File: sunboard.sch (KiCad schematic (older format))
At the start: 24 parts, among them J1 Barrel_Jack_MountingPin, J2 Conn_01x02, Q1 IRLB8721PBF, SW1 SW_Push, U1 STM32F030C8Tx, U4 MIC5209, Y1 Crystal_Small

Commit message: fixed footprints
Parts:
- removed J1: Barrel_Jack_MountingPin, Connector_BarrelJack:BarrelJack_CUI_PJ-063AH_Horizontal, symbol Connector:Barrel_Jack_MountingPin
- removed Q1: IRLB8721PBF, Package_TO_SOT_THT:TO-220-3_Vertical, symbol Transistor_FET:IRLB8721PBF
- added J3: Barrel_Jack, Connector_BarrelJack:BarrelJack_Horizontal, symbol Connector:Barrel_Jack
- 0.1uF1: footprint Capacitor_SMD:C_0603_1608Metric -> Capacitor_SMD:C_0805_2012Metric
- Y1: symbol Device:Crystal_Small -> Device:Crystal_GND24
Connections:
- net +12V: now also J3.1
- net GND: now also Y1.2, Y1.4, J3.2
- net at 1M1.2, 20pF2.1, U1.6 (PF1): now also Y1.3; no longer Y1.2
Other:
- moved on the sheet: FDD8780
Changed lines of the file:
@@
 $EndDescr
-$Comp
-L Transistor_FET:IRLB8721PBF Q1
-U 1 1 5C4B2BC1
-P 3000 1950
-F 0 "Q1" H 3205 1996 50  0000 L CNN
-F 1 "IRLB8721PBF" H 3205 1905 50  0000 L CNN
-F 2 "Package_TO_SOT_THT:TO-220-3_Vertical" H 3250 1875 50  0001 L CIN
-F 3 "http://www.infineon.com/dgdl/irlb8721pbf.pdf?fileId=5546d462533600a40153566056732591" H 3000 1950 50  0001 L CNN
-	1    3000 1950
-	1    0    0    -1
-$EndComp
-$Comp
-L Connector:Barrel_Jack_MountingPin J1
-U 1 1 5C4B7F75
-P 1250 1700
-F 0 "J1" H 1305 2017 50  0000 C CNN
-F 1 "Barrel_Jack_MountingPin" H 1305 1926 50  0000 C CNN
-F 2 "Connector_BarrelJack:BarrelJack_CUI_PJ-063AH_Horizontal" H 1300 1660 50  0001 C CNN
-F 3 "~" H 1300 1660 50  0001 C CNN
-	1    1250 1700
-	1    0    0    -1
-$EndComp
-$Comp
-L power:+12V #PWR0107
-U 1 1 5C4B8002
-P 1550 1600
-F 0 "#PWR0107" H 1550 1450 50  0001 C CNN
-F 1 "+12V" V 1565 1728 50  0000 L CNN
-F 2 "" H 1550 1600 50  0001 C CNN
-F 3 "" H 1550 1600 50  0001 C CNN
-	1    1550 1600
-	0    1    1    0
-$EndComp
-$Comp
-L power:GND #PWR0110
-U 1 1 5C4B822C
-P 1250 2000
-F 0 "#PWR0110" H 1250 1750 50  0001 C CNN
-F 1 "GND" H 1255 1827 50  0000 C CNN
-F 2 "" H 1250 2000 50  0001 C CNN
-F 3 "" H 1250 2000 50  0001 C CNN
-	1    1250 2000
-	1    0    0    -1
-$EndComp
-$Comp
-L power:GND #PWR0111
-U 1 1 5C4B824B
-P 1550 1800
-F 0 "#PWR0111" H 1550 1550 50  0001 C CNN
-F 1 "GND" H 1555 1627 50  0000 C CNN
-F 2 "" H 1550 1800 50  0001 C CNN
-F 3 "" H 1550 1800 50  0001 C CNN
-	1    1550 1800
-	1    0    0    -1
-$EndComp
 $Comp
 L power:GND #PWR0112
@@
 $EndComp
 $Comp
-L power:GND #PWR0113
-U 1 1 5C4B88F2
-P 3100 2150
-F 0 "#PWR0113" H 3100 1900 50  0001 C CNN
-F 1 "GND" H 3105 1977 50  0000 C CNN
-F 2 "" H 3100 2150 50  0001 C CNN
-F 3 "" H 3100 2150 50  0001 C CNN
-	1    3100 2150
-	1    0    0    -1
-$EndComp
-Wire Wire Line
-	3100 1750 3100 1400
-$Comp
 L MCU_ST_STM32F0:STM32F030C8Tx U1
 U 1 1 5C4B8CC2
@@
 	2050 5100 2250 5100
 $Comp
-L Device:Crystal_Small Y1
+L Device:Crystal_GND24 Y1
 U 1 1 5C4BE6CB
 P 1850 4450
@@
 Wire Wire Line
 	1500 4350 1300 4350
-Wire Wire Line
-	1300 4350 1300 4550
 Connection ~ 1300 4550
 Wire Wire Line
@@
 Text Label 4150 6200 0    50   ~ 0
 PWM
-Wire Wire Line
-	2800 1950 2350 1950
-Text Label 2350 1950 0    50   ~ 0
-PWM
-Text Label 3100 1400 0    50   ~ 0
-LED_GND
 $Comp
 L genLib:MIC5209 U4
@@
 F 0 "0.1uF1" H 4715 1596 50  0000 L CNN
 F 1 "C" H 4715 1505 50  0000 L CNN
-F 2 "Capacitor_SMD:C_0603_1608Metric" H 4638 1400 50  0001 C CNN
+F 2 "Capacitor_SMD:C_0805_2012Metric" H 4638 1400 50  0001 C CNN
 F 3 "~" H 4600 1550 50  0001 C CNN
 	1    4600 1550
@@
 Connection ~ 5150 1700
 Wire Wire Line
-	3900 1750 3900 1400
+	3200 1750 3200 1400
 $Comp
 L power:GND #PWR0122
 U 1 1 5C546FCB
-P 3900 2150
-F 0 "#PWR0122" H 3900 1900 50  0001 C CNN
-F 1 "GND" H 3905 1977 50  0000 C CNN
-F 2 "" H 3900 2150 50  0001 C CNN
-F 3 "" H 3900 2150 50  0001 C CNN
-	1    3900 2150
-	1    0    0    -1
-$EndComp
-Wire Wire Line
-	3600 1950 3450 1950
-Text Label 3450 1950 0    50   ~ 0
+P 3200 2150
+F 0 "#PWR0122" H 3200 1900 50  0001 C CNN
+F 1 "GND" H 3205 1977 50  0000 C CNN
+F 2 "" H 3200 2150 50  0001 C CNN
+F 3 "" H 3200 2150 50  0001 C CNN
+	1    3200 2150
+	1    0    0    -1
+$EndComp
+Wire Wire Line
+	2900 1950 2750 1950
+Text Label 2750 1950 0    50   ~ 0
 PWM
-Text Label 3900 1400 0    50   ~ 0
+Text Label 3200 1400 0    50   ~ 0
 LED_GND
 $Comp
 L Device:Q_NMOS_GDS FDD8780
 U 1 1 5C548B70
-P 3800 1950
-F 0 "FDD8780" H 4005 1996 50  0000 L CNN
-F 1 "Q_NMOS_GDS" H 4005 1905 50  0000 L CNN
-F 2 "Package_TO_SOT_SMD:TO-252-2" H 4000 2050 50  0001 C CNN
-F 3 "~" H 3800 1950 50  0001 C CNN
-	1    3800 1950
+P 3100 1950
+F 0 "FDD8780" H 3305 1996 50  0000 L CNN
+F 1 "Q_NMOS_GDS" H 3305 1905 50  0000 L CNN
+F 2 "Package_TO_SOT_SMD:TO-252-2" H 3300 2050 50  0001 C CNN
+F 3 "~" H 3100 1950 50  0001 C CNN
+	1    3100 1950
 	1    0    0    -1
 $EndComp
@@
 Text Label 6050 4300 0    50   ~ 0
 BOOT0
+$Comp
+L Connector:Barrel_Jack J3
+U 1 1 5C54AA5D
+P 1650 1650
+F 0 "J3" H 1705 1975 50  0000 C CNN
+F 1 "Barrel_Jack" H 1705 1884 50  0000 C CNN
+F 2 "Connector_BarrelJack:BarrelJack_Horizontal" H 1700 1610 50  0001 C CNN
+F 3 "~" H 1700 1610 50  0001 C CNN
+	1    1650 1650
+	1    0    0    -1
+$EndComp
+$Comp
+L power:+12V #PWR0107
+U 1 1 5C54AE42
+P 1950 1550
+F 0 "#PWR0107" H 1950 1400 50  0001 C CNN
+F 1 "+12V" V 1965 1678 50  0000 L CNN
+F 2 "" H 1950 1550 50  0001 C CNN
+F 3 "" H 1950 1550 50  0001 C CNN
+	1    1950 1550
+	0    1    1    0
+$EndComp
+$Comp
+L power:GND #PWR0110
+U 1 1 5C54AE7F
+P 1950 1750
+F 0 "#PWR0110" H 1950 1500 50  0001 C CNN
+F 1 "GND" H 1955 1577 50  0000 C CNN
+F 2 "" H 1950 1750 50  0001 C CNN
+F 3 "" H 1950 1750 50  0001 C CNN
+	1    1950 1750
+	1    0    0    -1
+$EndComp
+Wire Wire Line
+	2050 4450 1650 4450
+Wire Wire Line
+	1300 4350 1300 4450
+Connection ~ 1300 4450
+Wire Wire Line
+	1300 4450 1300 4550
+Connection ~ 1650 4450
+Wire Wire Line
+	1650 4450 1300 4450
 $EndSCHEMATC

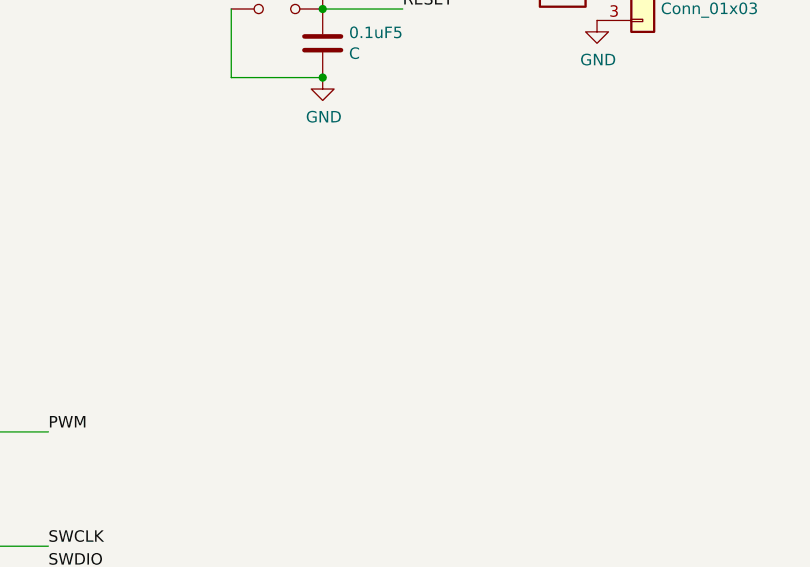
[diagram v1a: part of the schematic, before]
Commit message: routed everything and added programming headers
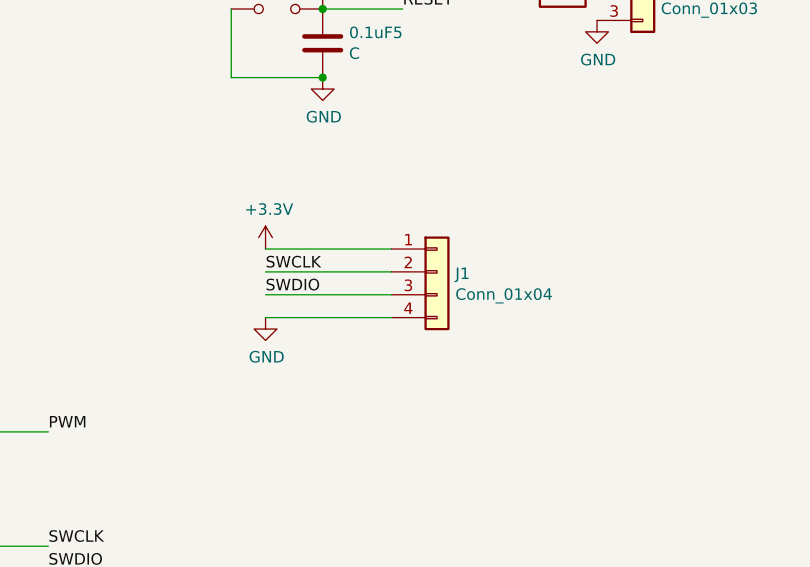
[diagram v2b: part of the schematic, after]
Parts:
- added J1: Conn_01x04, Connector_PinHeader_2.54mm:PinHeader_1x04_P2.54mm_Vertical, symbol Connector_Generic:Conn_01x04
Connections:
- net +3V3: now also J1.1 (Pin_1)
- net GND: now also J1.4 (Pin_4)
- net SWCLK: now also J1.2 (Pin_2)
- net SWDIO: now also J1.3 (Pin_3)
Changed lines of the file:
@@
 Wire Wire Line
 	1650 4450 1300 4450
+$Comp
+L Connector_Generic:Conn_01x04 J1
+U 1 1 5C547CE9
+P 5850 5500
+F 0 "J1" H 5930 5492 50  0000 L CNN
+F 1 "Conn_01x04" H 5930 5401 50  0000 L CNN
+F 2 "Connector_PinHeader_2.54mm:PinHeader_1x04_P2.54mm_Vertical" H 5850 5500 50  0001 C CNN
+F 3 "~" H 5850 5500 50  0001 C CNN
+	1    5850 5500
+	1    0    0    -1
+$EndComp
+Wire Wire Line
+	5650 5400 5100 5400
+Wire Wire Line
+	5650 5500 5100 5500
+Wire Wire Line
+	5650 5600 5100 5600
+Wire Wire Line
+	5650 5700 5100 5700
+$Comp
+L power:+3.3V #PWR0111
+U 1 1 5C54DC87
+P 5100 5400
+F 0 "#PWR0111" H 5100 5250 50  0001 C CNN
+F 1 "+3.3V" H 5115 5573 50  0000 C CNN
+F 2 "" H 5100 5400 50  0001 C CNN
+F 3 "" H 5100 5400 50  0001 C CNN
+	1    5100 5400
+	1    0    0    -1
+$EndComp
+$Comp
+L power:GND #PWR0113
+U 1 1 5C54DCC2
+P 5100 5700
+F 0 "#PWR0113" H 5100 5450 50  0001 C CNN
+F 1 "GND" H 5105 5527 50  0000 C CNN
+F 2 "" H 5100 5700 50  0001 C CNN
+F 3 "" H 5100 5700 50  0001 C CNN
+	1    5100 5700
+	1    0    0    -1
+$EndComp
+Text Label 5100 5500 0    50   ~ 0
+SWCLK
+Text Label 5100 5600 0    50   ~ 0
+SWDIO
 $EndSCHEMATC

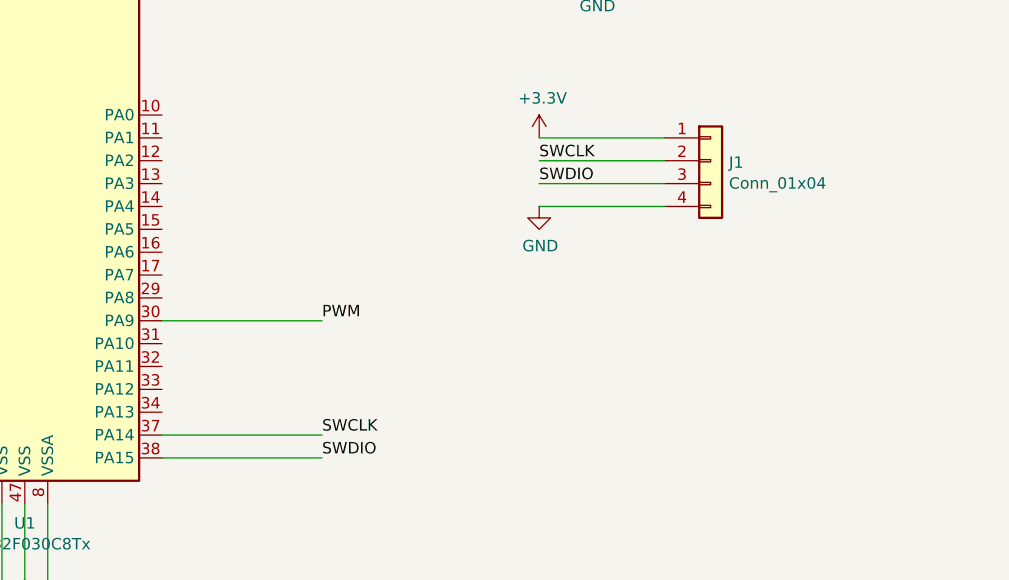
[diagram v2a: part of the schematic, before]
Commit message: added extra header for two GPIOs
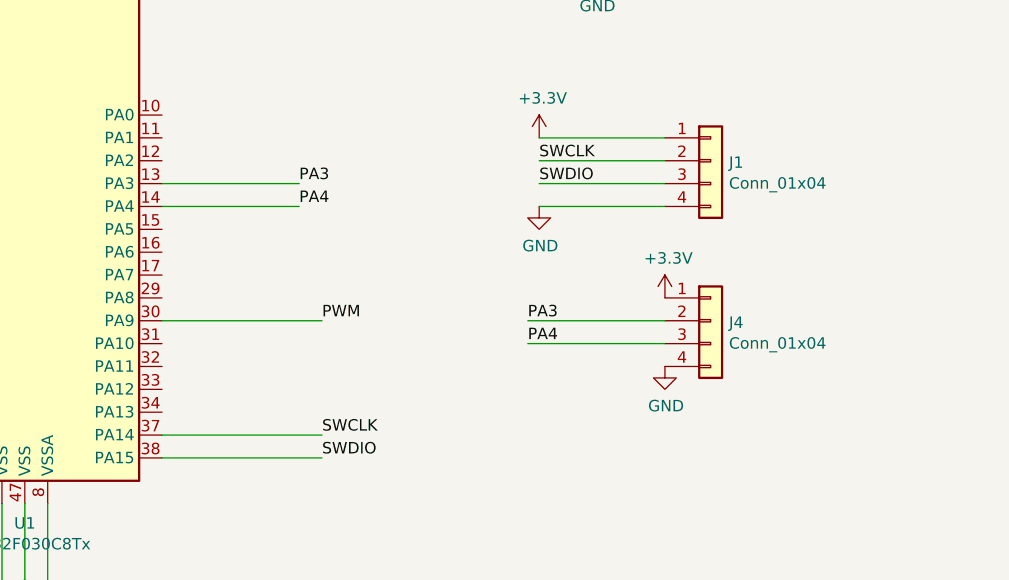
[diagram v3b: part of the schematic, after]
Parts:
- added J4: Conn_01x04, Connector_PinHeader_2.54mm:PinHeader_1x04_P2.54mm_Vertical, symbol Connector_Generic:Conn_01x04
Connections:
- net +3V3: now also J4.1 (Pin_1)
- net GND: now also J4.4 (Pin_4)
- net PA3: now reaches U1.13 (PA3)
- net PA3: now also J4.2 (Pin_2)
- net PA4: now reaches U1.14 (PA4)
- net PA4: now also J4.3 (Pin_3)
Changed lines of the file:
@@
 Text Label 5100 5600 0    50   ~ 0
 SWDIO
+$Comp
+L Connector_Generic:Conn_01x04 J4
+U 1 1 5C54E409
+P 5850 6200
+F 0 "J4" H 5930 6192 50  0000 L CNN
+F 1 "Conn_01x04" H 5930 6101 50  0000 L CNN
+F 2 "Connector_PinHeader_2.54mm:PinHeader_1x04_P2.54mm_Vertical" H 5850 6200 50  0001 C CNN
+F 3 "~" H 5850 6200 50  0001 C CNN
+	1    5850 6200
+	1    0    0    -1
+$EndComp
+$Comp
+L power:+3.3V #PWR0123
+U 1 1 5C54E554
+P 5650 6100
+F 0 "#PWR0123" H 5650 5950 50  0001 C CNN
+F 1 "+3.3V" H 5665 6273 50  0000 C CNN
+F 2 "" H 5650 6100 50  0001 C CNN
+F 3 "" H 5650 6100 50  0001 C CNN
+	1    5650 6100
+	1    0    0    -1
+$EndComp
+$Comp
+L power:GND #PWR0124
+U 1 1 5C54E591
+P 5650 6400
+F 0 "#PWR0124" H 5650 6150 50  0001 C CNN
+F 1 "GND" H 5655 6227 50  0000 C CNN
+F 2 "" H 5650 6400 50  0001 C CNN
+F 3 "" H 5650 6400 50  0001 C CNN
+	1    5650 6400
+	1    0    0    -1
+$EndComp
+Wire Wire Line
+	5650 6200 5050 6200
+Wire Wire Line
+	5650 6300 5050 6300
+Wire Wire Line
+	3450 5600 4050 5600
+Wire Wire Line
+	3450 5700 4050 5700
+Text Label 5050 6200 0    50   ~ 0
+PA3
+Text Label 5050 6300 0    50   ~ 0
+PA4
+Text Label 4050 5600 0    50   ~ 0
+PA3
+Text Label 4050 5700 0    50   ~ 0
+PA4
 $EndSCHEMATC
